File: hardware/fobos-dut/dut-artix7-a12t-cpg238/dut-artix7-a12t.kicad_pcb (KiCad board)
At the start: 4 copper layers, 88.9 x 76.2 mm, 206 parts, among them J1 Target, J10 Barrel_Jack_Switch, J2 Pmod 2x6, J3 575-8, J4 Glitch, J5 Conn_01x02, J6 Measure, J7 0878321420, J8 575-8, J9 Measure, Q1 FDS9435A, Q2 MMBT3904, Q3 BSS138, Q4 BSS138, Q5 BSS138, Q6 BSS138, Q7 BSS138, Q8 MMBT3904, SW1 SW_DIP_x03, SW2 SW_DIP_x03, U1 XC7A12T-CPG238, U10 SP3003-04ATG, U11 SP3003-04ATG, U2 SP3003-04ATG, U3 SP3003-04ATG, U4 SP3003-04ATG, U5 INA225, U6 BGA2801, U7 TS3A5018DBQR, U8 LTC3569EFE#PBF, U9 IS25LP256D-JMLE

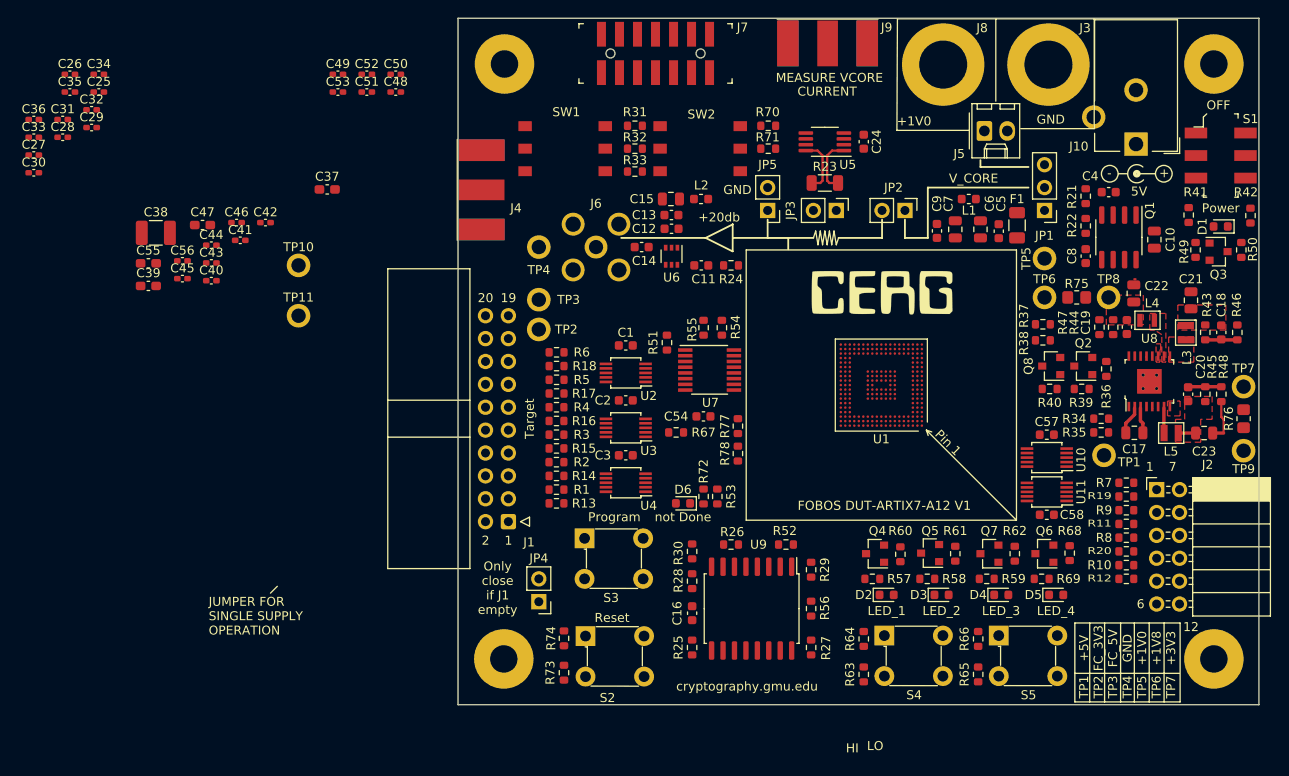
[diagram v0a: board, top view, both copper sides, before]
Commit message: Moved bypass/coupling capacitors underneath the FPGA Started routing top layer using 10 mil tracks with 5 mil spacing
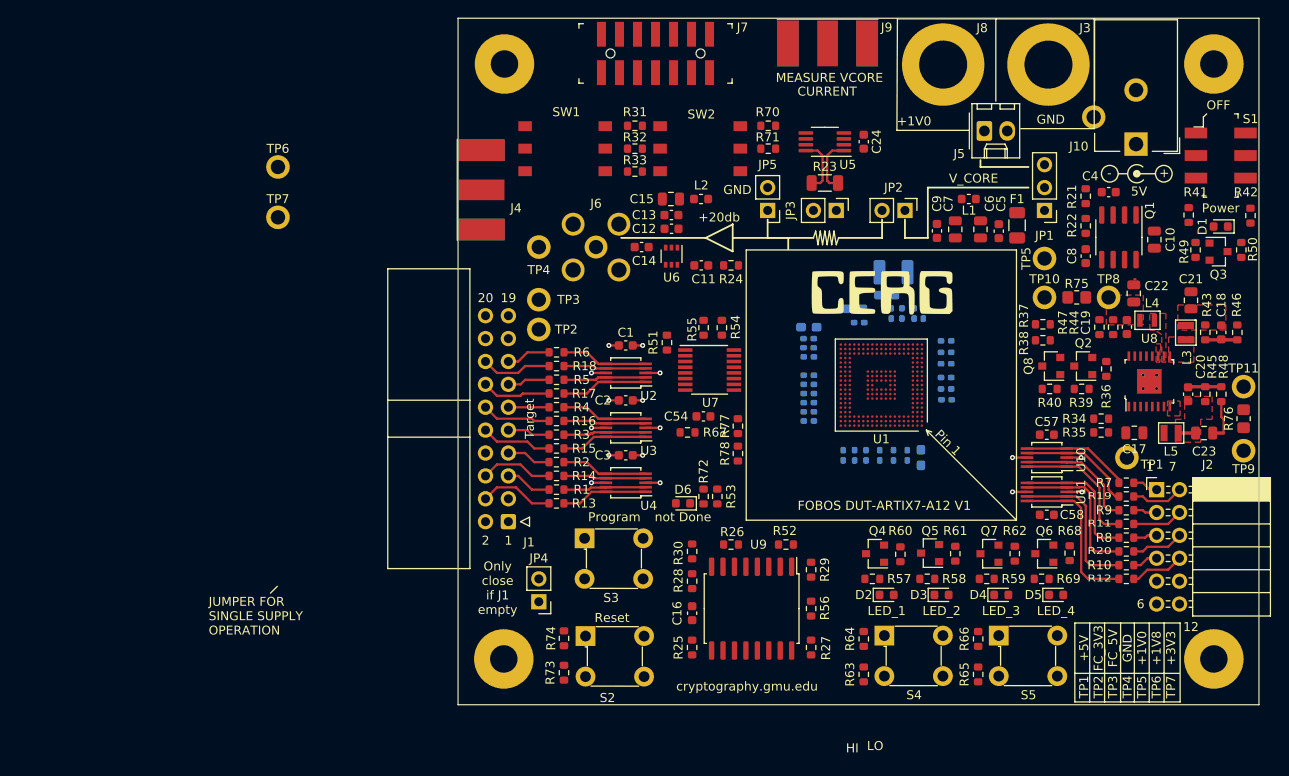
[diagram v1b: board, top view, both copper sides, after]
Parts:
- C25, C26, C27, C28, C29, C30, C31, C32, C33, C34, C35, C36, C37, C38, C39, C40, C41, C42, C43, C44, C45, C46, C47, C48, C49, C50, C51, C52, C53, C55, C56: moved to B.Cu
- moved TP7 108.8 mm to (-20.0, 18.5)
- moved TP11 105.2 mm to (87.2, 37.3)
- moved C36 102.5 mm to (48.3, 44.9), turned to 270 degrees
- moved C30 101.9 mm to (49.9, 44.9), turned to 270 degrees
- moved C31 98.1 mm to (46.8, 44.9), turned to 270 degrees
- moved C26 96.8 mm to (44.0, 44.9), turned to 270 degrees
- moved C28 95.9 mm to (45.3, 44.9), turned to 270 degrees
- moved C34 92.8 mm to (42.7, 44.9), turned to 270 degrees
- moved C27 90.6 mm to (38.9, 40.1), turned to 180 degrees
- moved C33 90.3 mm to (38.9, 37.0), turned to 180 degrees
- moved C35 87.8 mm to (38.9, 36.0), turned to 180 degrees
- moved C25 86.9 mm to (38.9, 41.1), turned to 180 degrees
- moved TP6 86.3 mm to (-20.0, 12.9)
- moved C32 85.6 mm to (38.9, 38.0), turned to 180 degrees
- moved C29 85.3 mm to (38.9, 39.0), turned to 180 degrees
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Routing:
- net JA10: track 0.00 -> 18.0 mm
- net JA4: track 0.00 -> 16.9 mm
- net JA9: track 0.00 -> 16.7 mm
- net JA3: track 0.00 -> 15.4 mm
- net JA8: track 0.00 -> 14.9 mm
- net JA2: track 0.00 -> 13.8 mm
- net JA7: track 0.00 -> 13.0 mm
- net JA1: track 0.00 -> 12.0 mm
- net FC_3V3: track 0.00 -> 11.4 mm, vias 0 -> 8
- net FC_IO: track 0.00 -> 9.60 mm
- net FC_DIO0: track 0.00 -> 9.60 mm
- net FC2D_HS: track 0.00 -> 9.60 mm
- net FD2C_CLK: track 0.00 -> 9.60 mm
- net FC_PROG: track 0.00 -> 9.59 mm
- net FC_DIO2: track 0.00 -> 9.59 mm
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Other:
- net class Default: clearance 0.0762 -> 0.127
- rule trace_clearance: 0.0762 -> 0.127

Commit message: Continued to work on layout, escaped FPGA power connections, routed mux signal near fpga.
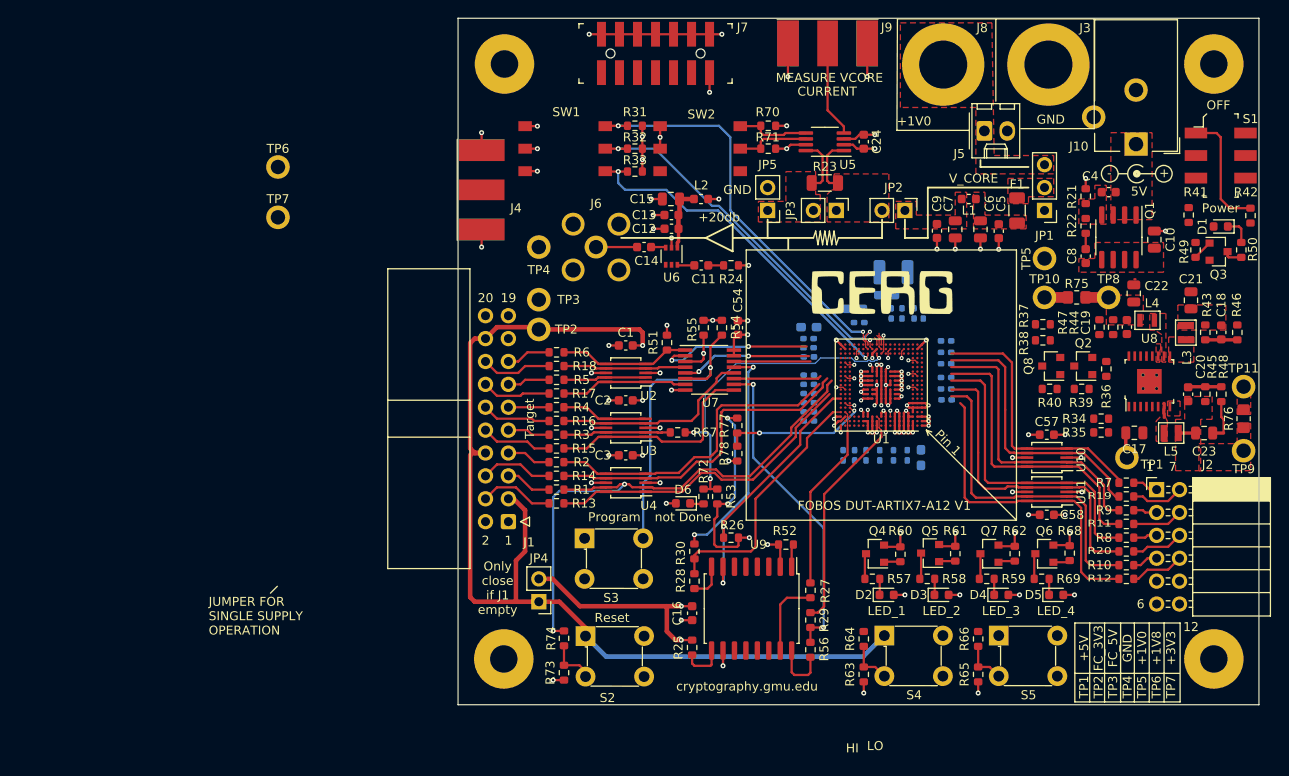
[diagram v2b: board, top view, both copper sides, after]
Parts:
- moved C54 10.6 mm to (31.1, 30.7), turned to 90 degrees
- moved R27 6.35 mm to (39.1, 59.9)
- moved R29 5.59 mm to (39.1, 63.2)
- moved R56 4.57 mm to (39.1, 66.5)
- moved F1 1.64 mm to (62.1, 17.7)
- moved R67 1.09 mm to (24.4, 42.4)
- moved R26 0.76 mm to (30.3, 54.0)
- moved C14 0.27 mm to (20.7, 21.8)
- moved R28 0.25 mm to (26.2, 58.9)
- moved R30 0.25 mm to (26.2, 55.6)
- moved R77 0.10 mm to (31.0, 41.6)
- moved R78 0.08 mm to (31.0, 44.7)
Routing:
- net FC_3V3: track 11.4 -> 274.4 mm, vias 8 -> 18
- net GND: track 16.2 -> 157.1 mm, vias 8 -> 85
- net +3V3: track 0.00 -> 138.4 mm, vias 0 -> 23
- net FC_5V: track 0.00 -> 134.8 mm
- net FC_RST: track 9.18 -> 61.2 mm, vias 0 -> 2
- net /FPGA Programming/MODE_0: track 0.00 -> 46.0 mm, vias 0 -> 2
- net /FPGA Programming/MODE_1: track 0.00 -> 41.2 mm, vias 0 -> 2
- net /FPGA Programming/MODE_2: track 0.00 -> 39.9 mm, vias 0 -> 2
- net SW_DONE: track 0.00 -> 36.6 mm, vias 0 -> 3
- net SW_CLK: track 0.00 -> 35.5 mm, vias 0 -> 2
- net SW_PROGRAM_B: track 0.00 -> 35.2 mm, vias 0 -> 2
- net /FPGA 1/FCS: track 0.00 -> 29.5 mm, vias 0 -> 2
- net /FPGA 1/DIN: track 0.00 -> 28.6 mm
- net FC2D_CLK: track 9.18 -> 36.9 mm
- net FD2C_CLK: track 9.60 -> 35.7 mm
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- added copper zone on F.Cu, net +3V3
- added copper zone on F.Cu, net /Power/SW3
- added copper zone on F.Cu, net FC_5V
- added copper zone on F.Cu, net Net-(C4-Pad2)
- added copper zone on F.Cu, net Net-(C5-Pad1)
- added copper zone on F.Cu, net Net-(C7-Pad1)
- added copper zone on F.Cu, net Net-(F1-Pad2)
- added copper zone on F.Cu, net Net-(J5-Pad1)
- added copper zone on F.Cu, net Net-(JP2-Pad2)
- added copper zone on F.Cu, net VCCINT

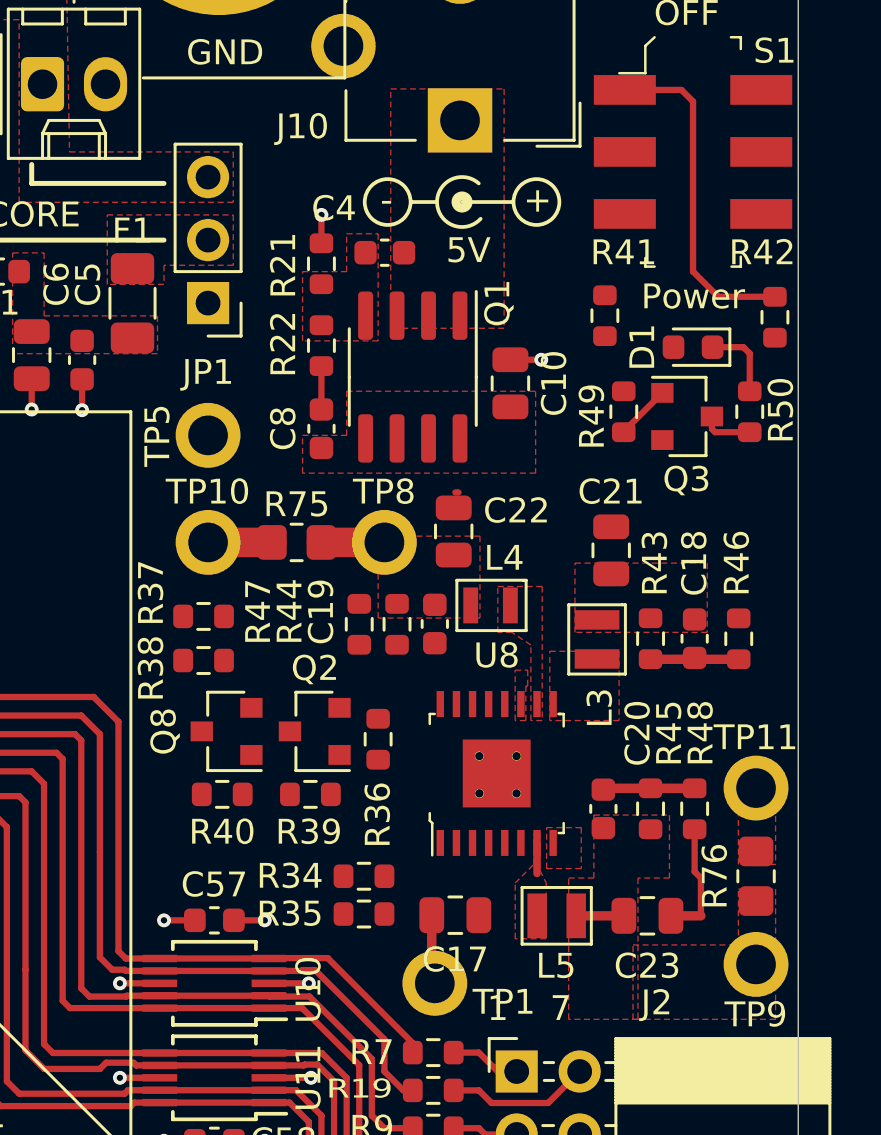
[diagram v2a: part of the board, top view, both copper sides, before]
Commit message: Continued to work on dut-artix7-a12t.kicad_pcb layout
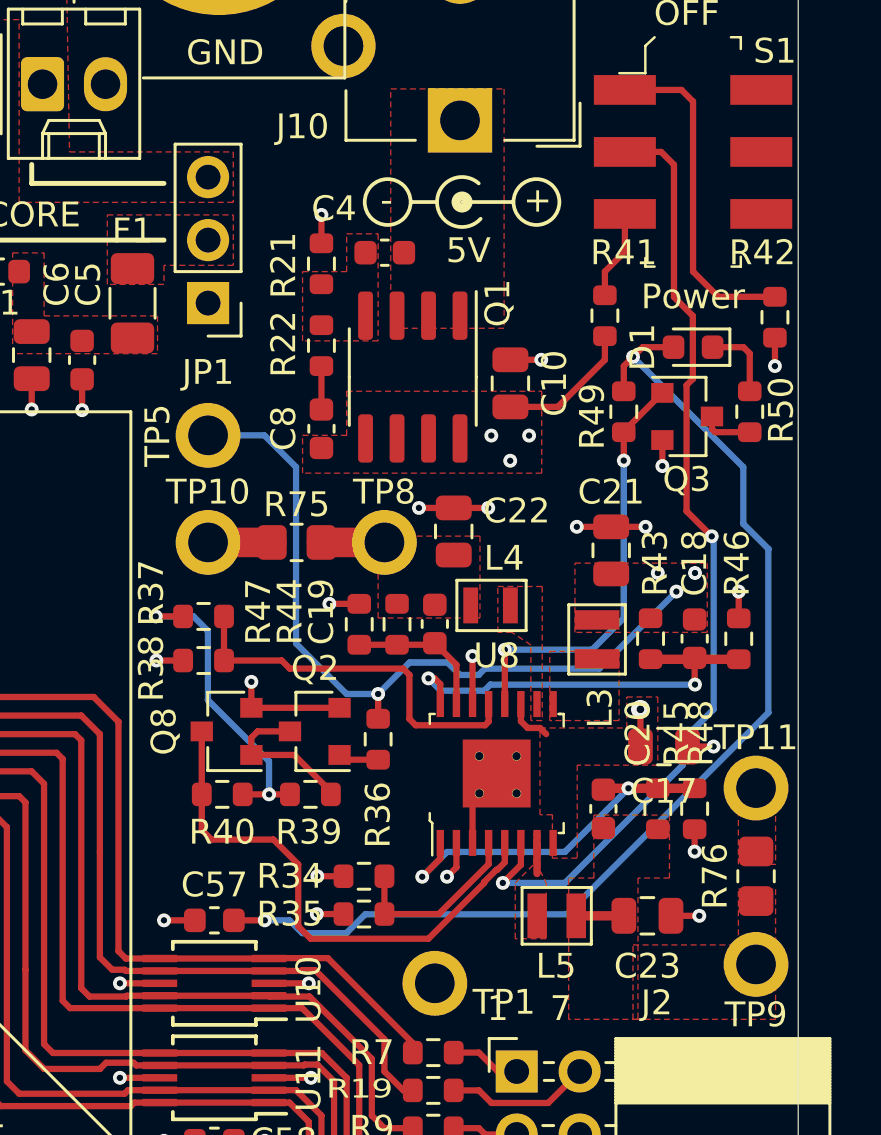
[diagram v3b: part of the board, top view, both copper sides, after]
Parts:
- moved C17 10.8 mm to (83.5, 35.6)
- moved R45 0.29 mm to (83.2, 38.1)
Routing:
- net +5V: track 2.80 -> 75.8 mm, vias 0 -> 8
- net FC_3V3: track 274.4 -> 339.7 mm, vias 18 -> 19
- net ON_OFF: track 0.00 -> 38.9 mm, vias 0 -> 2
- net +1V0: track 0.00 -> 30.5 mm, vias 0 -> 4
- net /Power/EN2: track 0.08 -> 21.6 mm
- net GND: track 157.1 -> 175.4 mm, vias 85 -> 99
- net /Power/MODE: track 0.08 -> 15.4 mm
- net PGOOD: track 2.23 -> 17.2 mm, vias 0 -> 2
- net /Power/FB1: track 3.56 -> 17.1 mm, vias 0 -> 2
- net /Power/FB3: track 3.70 -> 15.2 mm, vias 0 -> 2
- net /Power/EN3: track 0.00 -> 7.42 mm
- net Net-(Q2-Pad3): track 0.00 -> 6.29 mm
- net /Power/FB2: track 0.13 -> 5.89 mm
- net Net-(R41-Pad1): track 0.00 -> 3.61 mm
- net Net-(Q2-Pad1): track 0.00 -> 1.64 mm
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
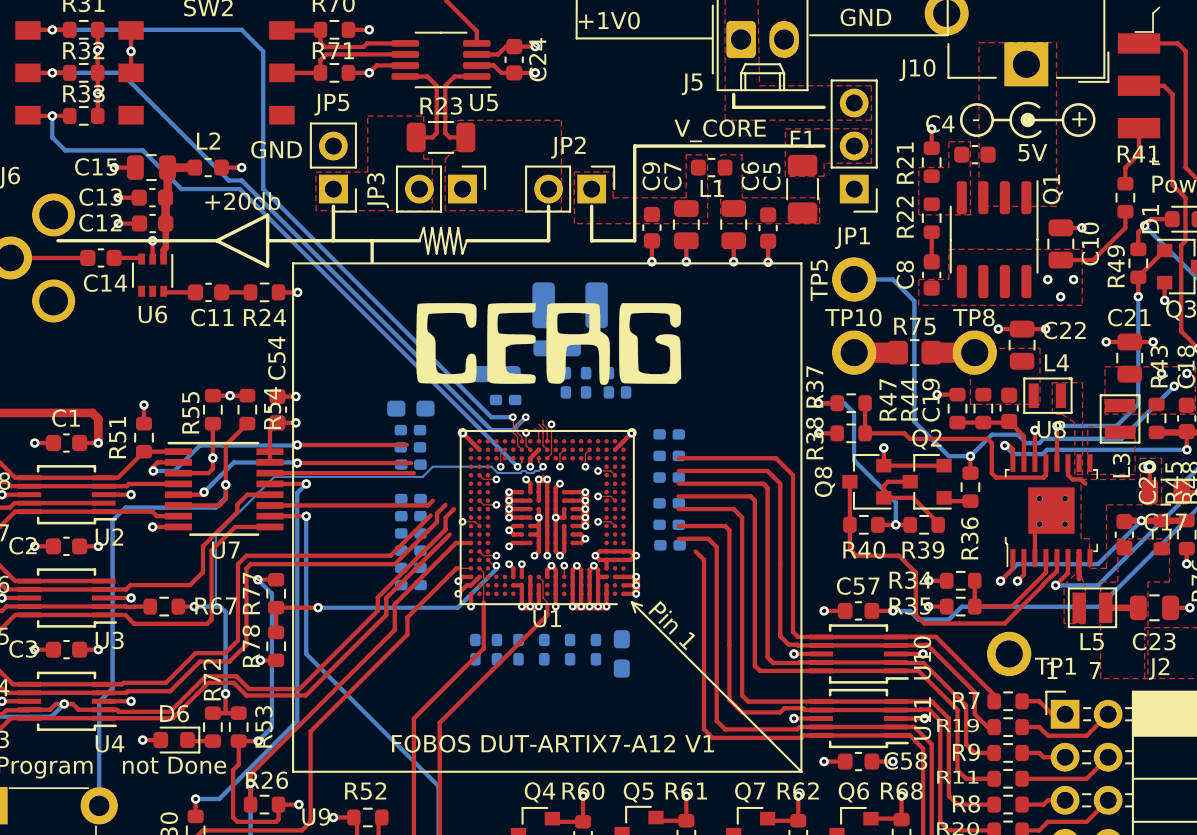
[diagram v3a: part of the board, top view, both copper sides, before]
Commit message: Updated escape routing of most pads to take advantage of "pad sacrifices"
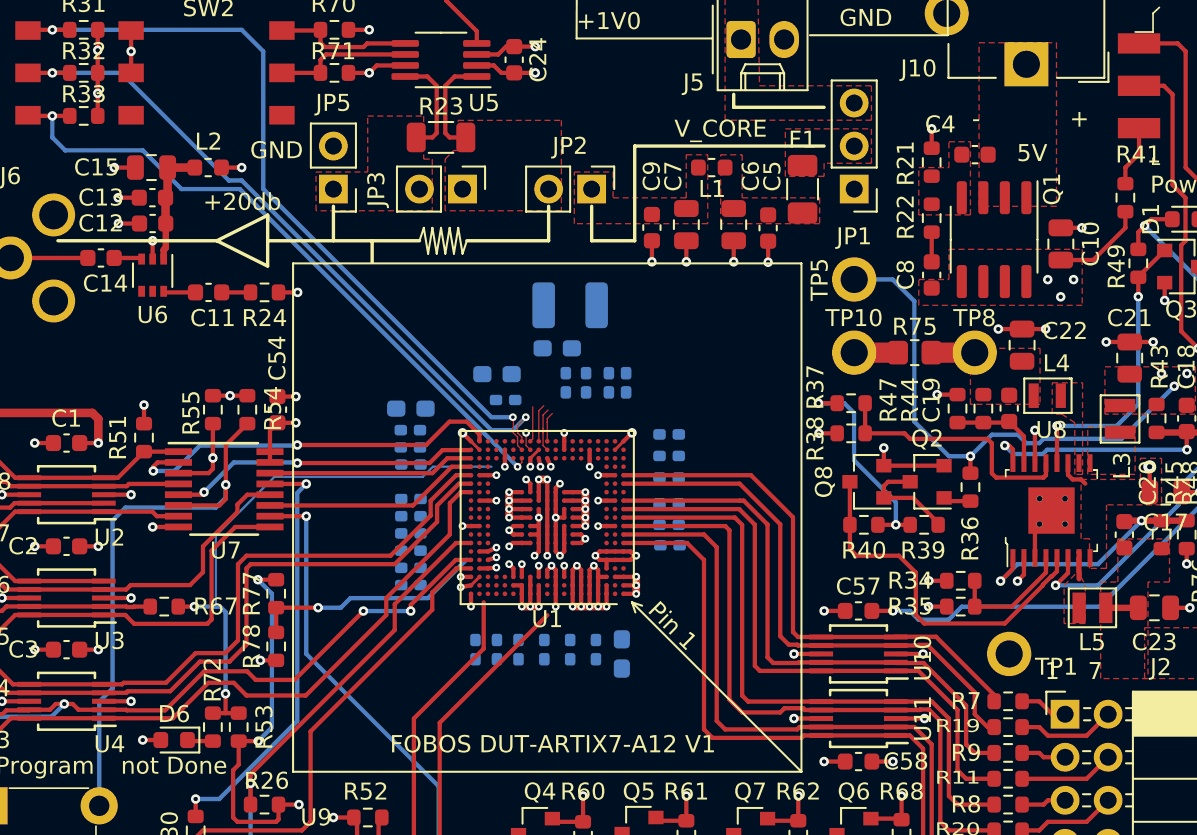
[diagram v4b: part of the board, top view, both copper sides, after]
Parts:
- removed G***: LOGO, fobos-shield:cerg_logo
- removed REF**: Symbol_Barrel_Polarity, Symbol:Symbol_Barrel_Polarity
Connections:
- U1 pad D17: Net-(U1-PadD17) -> /FPGA 1/MOSI
- U1 pad E19: Net-(U1-PadE19) -> FC_RST
- U1 pad F17: Net-(U1-PadF17) -> GND
- U1 pad G1: Net-(U1-PadG1) -> JA10
- U1 pad H1: Net-(U1-PadH1) -> JA4
- U1 pad J1: Net-(U1-PadJ1) -> JA9
- U1 pad J19: Net-(U1-PadJ19) -> GND
- U1 pad J3: Net-(U1-PadJ3) -> GND
- U1 pad K1: Net-(U1-PadK1) -> JA3
- U1 pad M17: Net-(U1-PadM17) -> GND
- U1 pad M3: Net-(U1-PadM3) -> GND
- U1 pad N19: Net-(U1-PadN19) -> FD2C_CLK
- U1 pad P19: Net-(U1-PadP19) -> FC2D_CLK
- U1 pad R17: Net-(U1-PadR17) -> GND
- U1 pad R19: Net-(U1-PadR19) -> FC_IO
- U1 pad R3: Net-(U1-PadR3) -> GND
- U1 pad T19: Net-(U1-PadT19) -> FC_DIO0_MUX
- U1 pad U15: Net-(U1-PadU15) -> GND
- U1 pad U19: Net-(U1-PadU19) -> FC_DIO1_MUX
- U1 pad U5: Net-(U1-PadU5) -> GND
- U1 pad V19: Net-(U1-PadV19) -> FC_DIO2_MUX
- U1 pad W18: Net-(U1-PadW18) -> FC_DIO3_MUX
- U1 pad W8: Net-(U1-PadW8) -> GND
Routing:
- net FC_DIO3_MUX: track 17.5 -> 23.0 mm
- net JA10: track 35.8 -> 40.3 mm
- net FC_IO: track 35.7 -> 39.5 mm
- net FC_DIO2_MUX: track 14.6 -> 18.4 mm
- net FC_DIO1_MUX: track 8.49 -> 12.2 mm
- net SW_DONE: track 36.6 -> 33.1 mm
- net FD2C_CLK: track 35.7 -> 39.1 mm
- net JA4: track 36.1 -> 39.5 mm
- net JA9: track 35.6 -> 38.9 mm
- net FC_DIO0_MUX: track 9.73 -> 12.8 mm
- net JA3: track 34.7 -> 37.5 mm
- net FC2D_CLK: track 36.9 -> 39.2 mm
- net JA8: track 33.3 -> 35.4 mm
- net SW_INIT_B: track 4.81 -> 6.90 mm
- net /FPGA 1/PUDC: track 16.3 -> 14.4 mm
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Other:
- net class Default: clearance 0.127 -> 0.0762
- rule trace_clearance: 0.127 -> 0.0762
